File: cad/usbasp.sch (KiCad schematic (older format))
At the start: 33 parts, among them J1 USB_B, J2 UISP, J3 SLOW-SCK, J4 SELF-PRG, SW1 5V-3V3, SW2 V-TARGET, U1 AMS1117-3.3, U2 ATmega88-20PU, Y1 12MHz

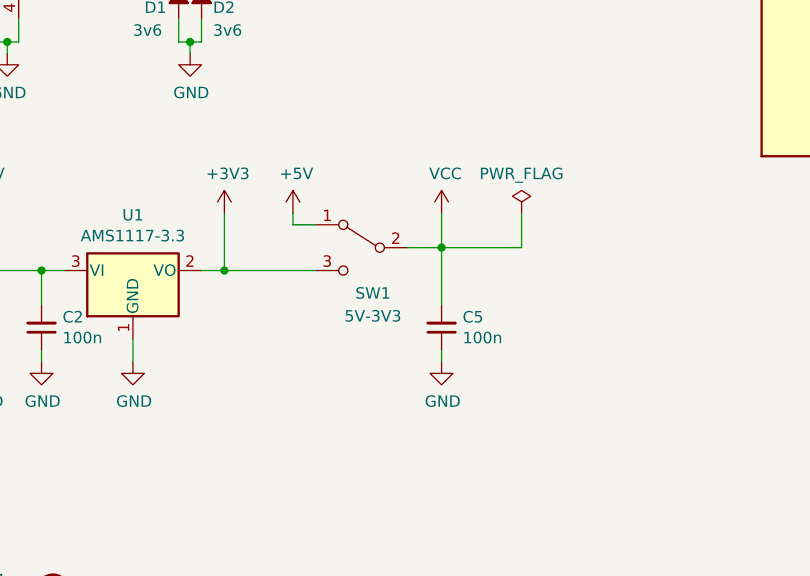
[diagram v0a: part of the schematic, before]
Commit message: Schematic: add 3.3v support
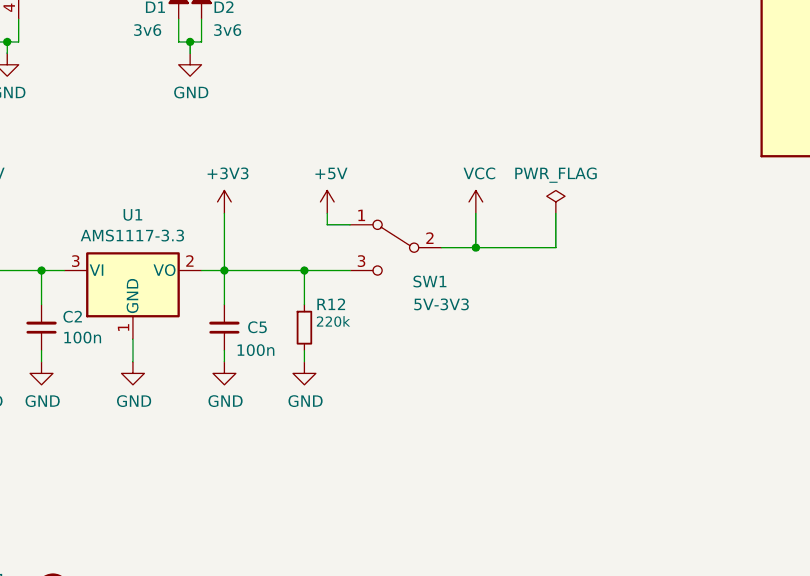
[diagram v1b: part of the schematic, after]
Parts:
- added R12: 220k, Resistor_SMD:R_1206_3216Metric_Pad1.42x1.75mm_HandSolder, symbol Device:R_Small
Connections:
- net +3V3: now also C5.2, R12.1
- net GND: now also R12.2
- net VCC: no longer C5.2
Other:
- moved on the sheet: C5, SW1
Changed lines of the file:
@@
 L Device:C_Small C5
 U 1 1 5EC2BD7C
-P 3850 5750
-F 0 "C5" H 3758 5704 50  0000 R CNN
-F 1 "100n" H 3758 5795 50  0000 R CNN
-F 2 "Capacitor_SMD:C_1206_3216Metric_Pad1.42x1.75mm_HandSolder" H 3850 5750 50  0001 C CNN
-F 3 "~" H 3850 5750 50  0001 C CNN
-	1    3850 5750
+P 2900 5750
+F 0 "C5" H 2800 5750 50  0000 R CNN
+F 1 "100n" H 2850 5850 50  0000 R CNN
+F 2 "Capacitor_SMD:C_1206_3216Metric_Pad1.42x1.75mm_HandSolder" H 2900 5750 50  0001 C CNN
+F 3 "~" H 2900 5750 50  0001 C CNN
+	1    2900 5750
 	-1   0    0    1
 $EndComp
@@
 L power:GND #PWR011
 U 1 1 5EC2C667
-P 3850 5900
-F 0 "#PWR011" H 3850 5650 50  0001 C CNN
-F 1 "GND" H 3855 5727 50  0000 C CNN
-F 2 "" H 3850 5900 50  0001 C CNN
-F 3 "" H 3850 5900 50  0001 C CNN
-	1    3850 5900
-	1    0    0    -1
-$EndComp
-Wire Wire Line
-	3850 5900 3850 5850
+P 2900 5900
+F 0 "#PWR011" H 2900 5650 50  0001 C CNN
+F 1 "GND" H 2905 5727 50  0000 C CNN
+F 2 "" H 2900 5900 50  0001 C CNN
+F 3 "" H 2900 5900 50  0001 C CNN
+	1    2900 5900
+	1    0    0    -1
+$EndComp
 Connection ~ 2900 5500
 $Comp
@@
 L Switch:SW_SPDT SW1
 U 1 1 5EC32972
-P 3500 5400
-F 0 "SW1" H 3450 5200 50  0000 C CNN
-F 1 "5V-3V3" H 3450 5100 50  0000 C CNN
-F 2 "Connector_PinHeader_2.54mm:PinHeader_1x03_P2.54mm_Vertical" H 3500 5400 50  0001 C CNN
-F 3 "~" H 3500 5400 50  0001 C CNN
-	1    3500 5400
+P 3650 5400
+F 0 "SW1" H 3500 5250 50  0000 C CNN
+F 1 "5V-3V3" H 3450 5150 50  0000 C CNN
+F 2 "Connector_PinHeader_2.54mm:PinHeader_1x03_P2.54mm_Vertical" H 3650 5400 50  0001 C CNN
+F 3 "~" H 3650 5400 50  0001 C CNN
+	1    3650 5400
 	-1   0    0    -1
 $EndComp
@@
 L power:+5V #PWR012
 U 1 1 5EC45025
-P 3200 5250
-F 0 "#PWR012" H 3200 5100 50  0001 C CNN
-F 1 "+5V" H 3215 5423 50  0000 C CNN
-F 2 "" H 3200 5250 50  0001 C CNN
-F 3 "" H 3200 5250 50  0001 C CNN
-	1    3200 5250
-	1    0    0    -1
-$EndComp
-Wire Wire Line
-	3200 5250 3200 5300
-Wire Wire Line
-	3200 5300 3300 5300
-Wire Wire Line
-	3700 5400 3850 5400
-Wire Wire Line
-	3850 5400 3850 5250
+P 3350 5250
+F 0 "#PWR012" H 3350 5100 50  0001 C CNN
+F 1 "+5V" H 3365 5423 50  0000 C CNN
+F 2 "" H 3350 5250 50  0001 C CNN
+F 3 "" H 3350 5250 50  0001 C CNN
+	1    3350 5250
+	1    0    0    -1
+$EndComp
+Wire Wire Line
+	3350 5250 3350 5300
+Wire Wire Line
+	3350 5300 3450 5300
+Wire Wire Line
+	3850 5400 4000 5400
+Wire Wire Line
+	4000 5400 4000 5250
 $Comp
 L power:VCC #PWR014
 U 1 1 5EC4A1DC
-P 3850 5250
-F 0 "#PWR014" H 3850 5100 50  0001 C CNN
-F 1 "VCC" H 3867 5423 50  0000 C CNN
-F 2 "" H 3850 5250 50  0001 C CNN
-F 3 "" H 3850 5250 50  0001 C CNN
-	1    3850 5250
-	1    0    0    -1
-$EndComp
-Wire Wire Line
-	2900 5500 3300 5500
+P 4000 5250
+F 0 "#PWR014" H 4000 5100 50  0001 C CNN
+F 1 "VCC" H 4017 5423 50  0000 C CNN
+F 2 "" H 4000 5250 50  0001 C CNN
+F 3 "" H 4000 5250 50  0001 C CNN
+	1    4000 5250
+	1    0    0    -1
+$EndComp
+Wire Wire Line
+	2900 5500 3250 5500
 Wire Wire Line
 	1850 5250 1850 5500
@@
 L power:PWR_FLAG #FLG01
 U 1 1 5EC504C4
-P 4200 5250
-F 0 "#FLG01" H 4200 5325 50  0001 C CNN
-F 1 "PWR_FLAG" H 4200 5423 50  0000 C CNN
-F 2 "" H 4200 5250 50  0001 C CNN
-F 3 "~" H 4200 5250 50  0001 C CNN
-	1    4200 5250
-	1    0    0    -1
-$EndComp
-Wire Wire Line
-	3850 5400 4200 5400
-Wire Wire Line
-	4200 5400 4200 5250
-Connection ~ 3850 5400
+P 4350 5250
+F 0 "#FLG01" H 4350 5325 50  0001 C CNN
+F 1 "PWR_FLAG" H 4350 5423 50  0000 C CNN
+F 2 "" H 4350 5250 50  0001 C CNN
+F 3 "~" H 4350 5250 50  0001 C CNN
+	1    4350 5250
+	1    0    0    -1
+$EndComp
+Wire Wire Line
+	4000 5400 4350 5400
+Wire Wire Line
+	4350 5400 4350 5250
+Connection ~ 4000 5400
 Text Label 6700 2500 2    44   ~ 0
 DATA+
@@
 Wire Wire Line
 	8250 4800 8550 4800
-Wire Wire Line
-	3850 5650 3850 5400
 $Comp
 L Connector_Generic:Conn_01x02 J4
@@
 	0    1    1    0
 $EndComp
+Wire Wire Line
+	2900 5850 2900 5900
+Wire Wire Line
+	2900 5650 2900 5500
+$Comp
+L Device:R_Small R12
+U 1 1 5EBF244B
+P 3250 5750
+F 0 "R12" H 3300 5850 50  0000 L CNN
+F 1 "220k" H 3300 5775 44  0000 L CNN
+F 2 "Resistor_SMD:R_1206_3216Metric_Pad1.42x1.75mm_HandSolder" H 3250 5750 50  0001 C CNN
+F 3 "~" H 3250 5750 50  0001 C CNN
+	1    3250 5750
+	1    0    0    -1
+$EndComp
+$Comp
+L power:GND #PWR0102
+U 1 1 5EBF7ACF
+P 3250 5900
+F 0 "#PWR0102" H 3250 5650 50  0001 C CNN
+F 1 "GND" H 3255 5727 50  0000 C CNN
+F 2 "" H 3250 5900 50  0001 C CNN
+F 3 "" H 3250 5900 50  0001 C CNN
+	1    3250 5900
+	1    0    0    -1
+$EndComp
+Wire Wire Line
+	3250 5650 3250 5500
+Connection ~ 3250 5500
+Wire Wire Line
+	3250 5500 3450 5500
+Wire Wire Line
+	3250 5850 3250 5900
 $EndSCHEMATC
